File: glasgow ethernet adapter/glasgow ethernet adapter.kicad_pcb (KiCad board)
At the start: 4 copper layers, 61.7 x 49 mm, 60 parts, among them J1 Glasgow Port, J2 RJ45_Amphenol_RJMG201K21120FR, U1 MxL86110, Y1 25 MHz

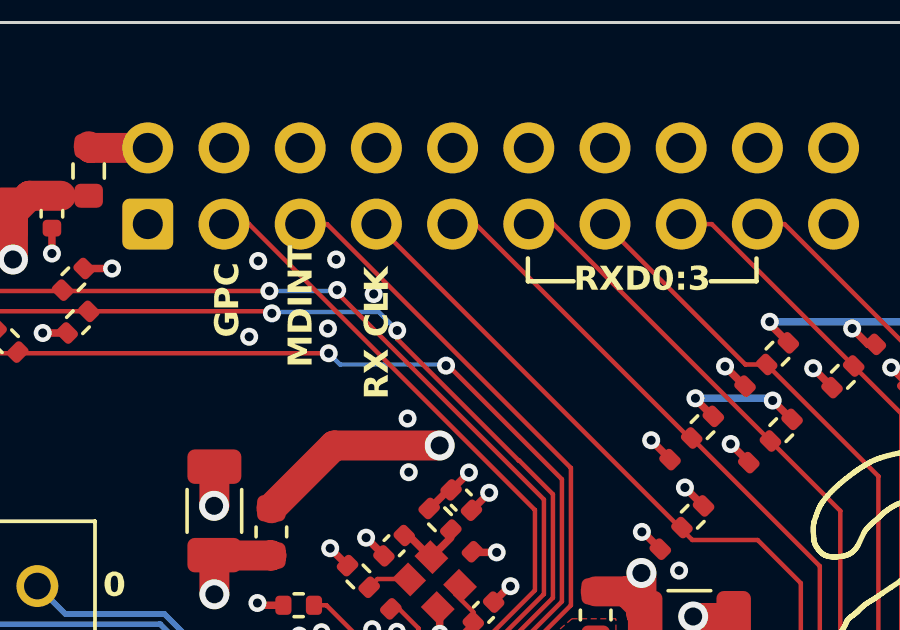
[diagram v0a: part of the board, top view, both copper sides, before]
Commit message: add RX_CTL silkscreen label
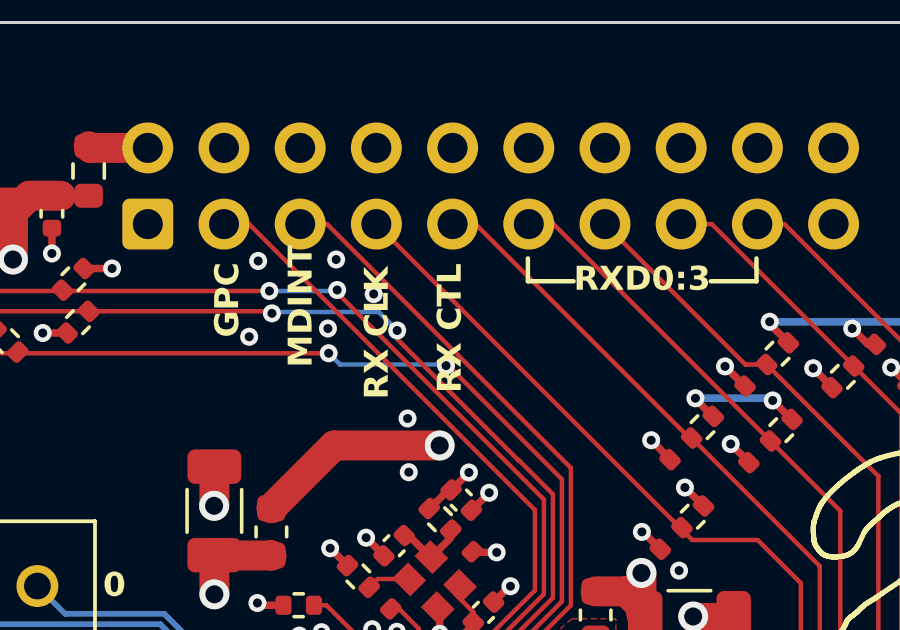
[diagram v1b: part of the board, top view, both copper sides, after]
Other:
- board text added: "RX CTL"
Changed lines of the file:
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@@
+		)
+	)
+	(gr_text "RX CTL\n"
+		(at 163.1 87.85 90)
+		(layer "F.SilkS")
+		(effects
+			(font
+				(size 0.8 0.8)
+				(thickness 0.15)
+				(bold yes)
+			)
+			(justify left bottom)
 		)
 	)

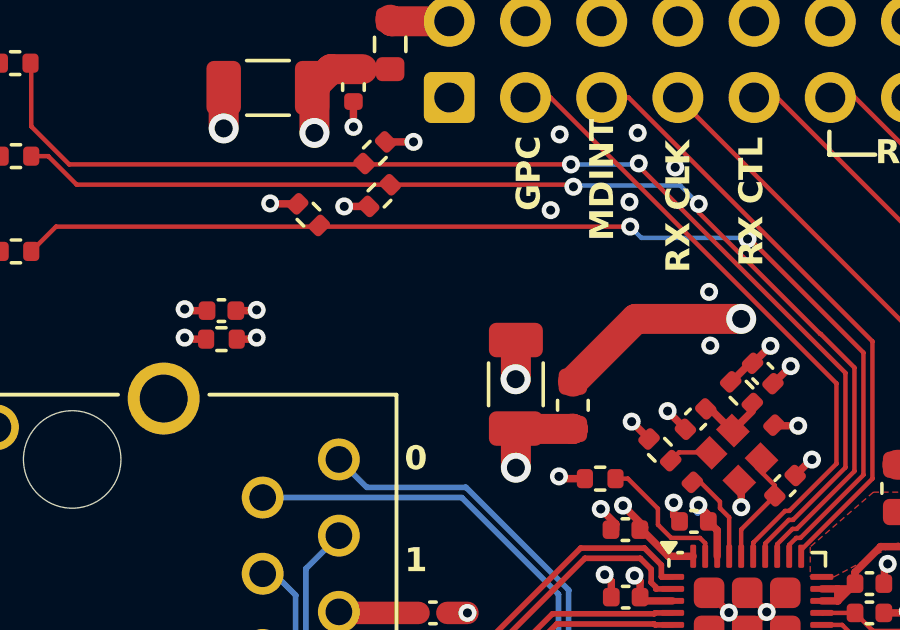
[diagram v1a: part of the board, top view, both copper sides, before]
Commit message: add 1v1 regulator
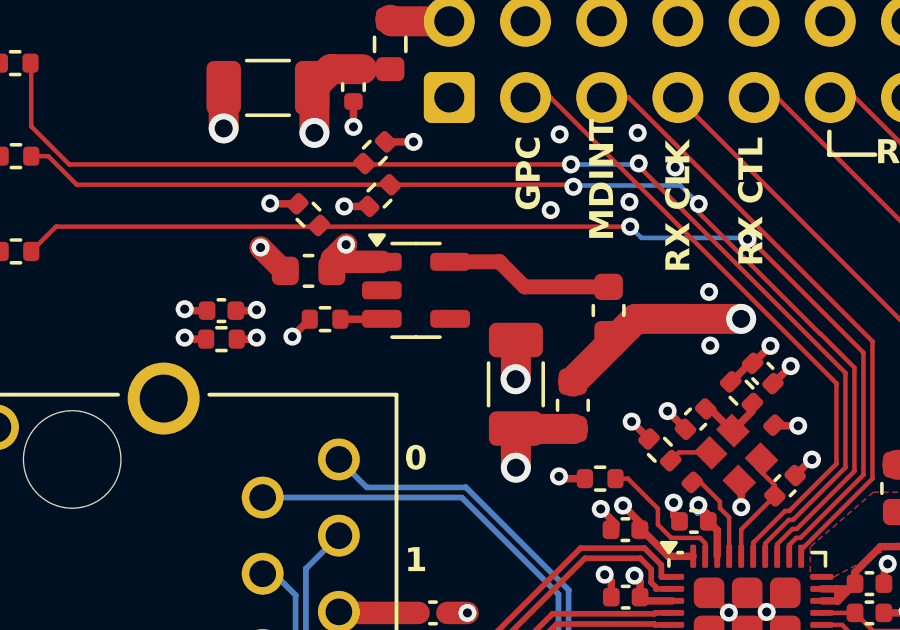
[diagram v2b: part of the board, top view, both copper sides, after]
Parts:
- added C16: 1u, Capacitor_SMD:C_0603_1608Metric, F.Cu at (147.9, 88.0)
- added L4: 2.2 uH, Inductor_SMD:L_0603_1608Metric, F.Cu at (157.9, 89.3)
- added R27: 4.7k, Resistor_SMD:R_0402_1005Metric, F.Cu at (148.4, 89.6)
- added U2: ~, Package_TO_SOT_SMD:SOT-23-5, F.Cu at (151.5, 88.6)
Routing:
- net Net-(U2-OUT): track 0.00 -> 5.64 mm
- net +3V3: track 36.0 -> 39.7 mm, vias 15 -> 17
- net Net-(U2-EN): track 0.00 -> 1.39 mm
- net GND: track 48.0 -> 49.2 mm, vias 50 -> 51

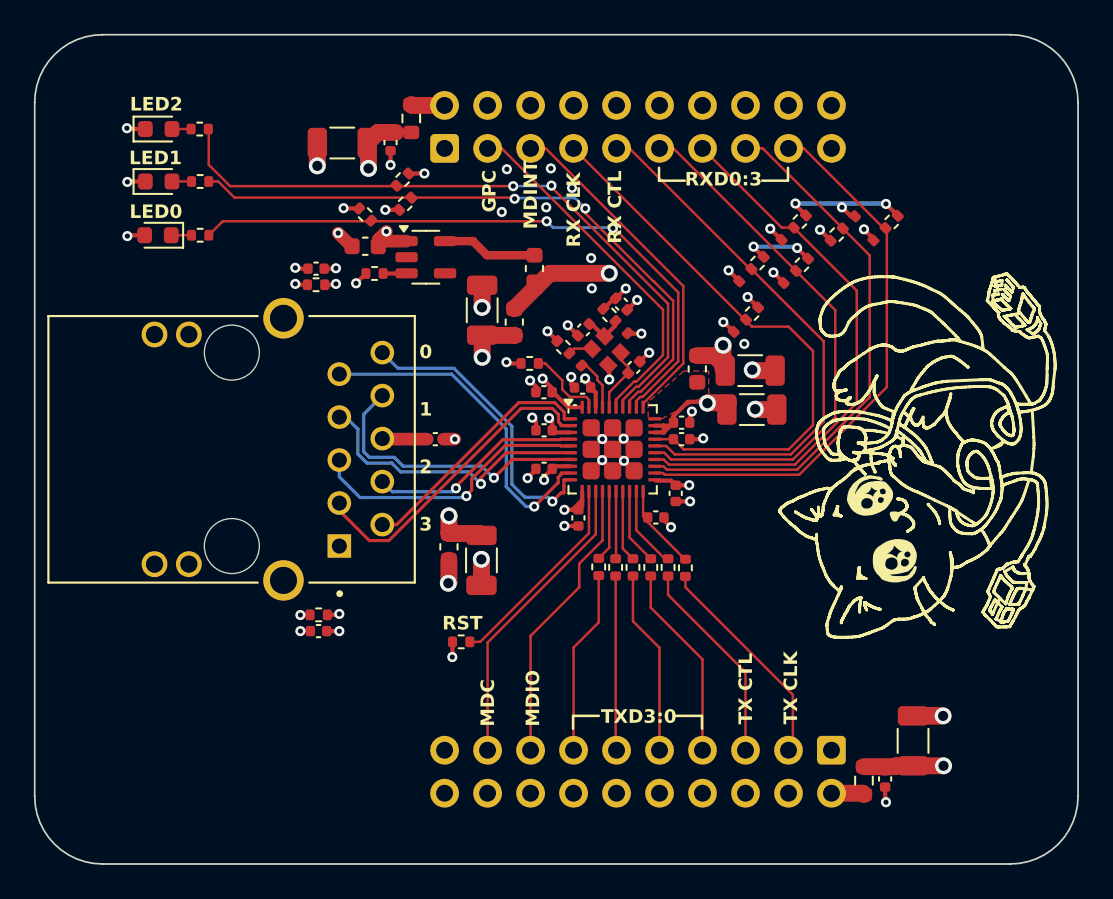
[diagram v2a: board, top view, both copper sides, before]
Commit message: swap MDC+MDIO with TXD0:3
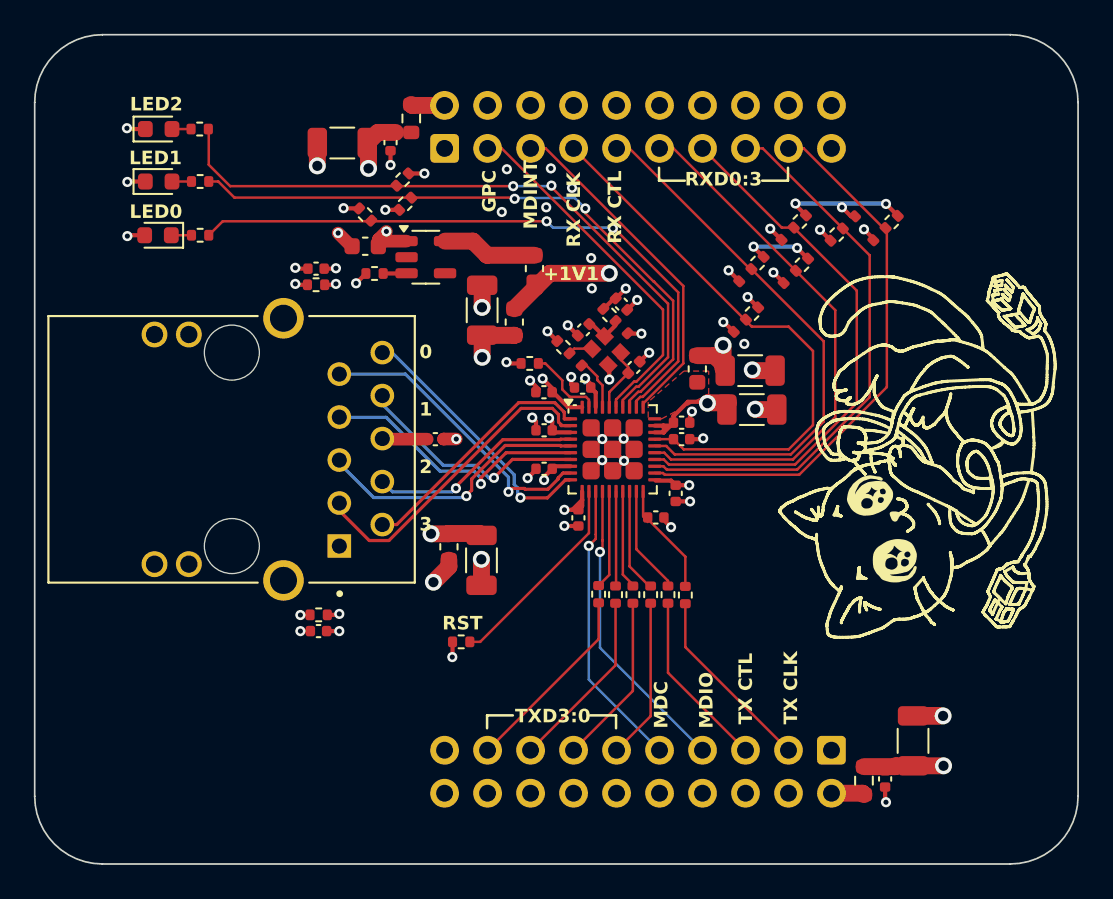
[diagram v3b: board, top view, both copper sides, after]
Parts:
- moved R15 1.61 mm to (161.7, 108.6)
- moved R16 1.61 mm to (162.7, 108.6)
- moved R23 1.61 mm to (166.8, 108.6)
- moved R20 1.61 mm to (163.7, 108.6)
- moved R21 1.61 mm to (164.7, 108.6)
- moved R22 1.61 mm to (165.8, 108.6)
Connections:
- J1 pad B2: /TXD0 -> /MDIO
- J1 pad B3: /TXD1 -> /MDC
- J1 pad B4: /TXD2 -> /TXD0
- J1 pad B5: /TXD3 -> /TXD1
- J1 pad B6: /MDIO -> /TXD2
- J1 pad B7: /MDC -> /TXD3
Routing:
- net /TRX3-: track 17.1 -> 13.9 mm
- net /TRX4+: track 20.4 -> 18.0 mm
- net /TRX4-: track 17.8 -> 15.7 mm
- net /TXD0: track 11.6 -> 9.60 mm
- net Net-(U1-TX_CLK): track 5.26 -> 7.15 mm
- net Net-(U1-TX_CTL): track 4.87 -> 6.55 mm
- net Net-(U1-TXD0): track 4.50 -> 6.16 mm
- net Net-(U1-TXD2): track 3.99 -> 5.60 mm
- net Net-(U1-TXD1): track 4.23 -> 5.83 mm
- net /TX_CTL: track 12.2 -> 10.6 mm
- net /TX_CLK: track 13.0 -> 11.6 mm
- net Net-(U1-TXD3): track 4.39 -> 5.82 mm
- net /MDIO: track 17.1 -> 17.9 mm, vias 0 -> 1
- net /TXD1: track 10.9 -> 10.1 mm
- net /MDC: track 17.9 -> 17.2 mm, vias 0 -> 1
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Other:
- board text added: "+1V1"

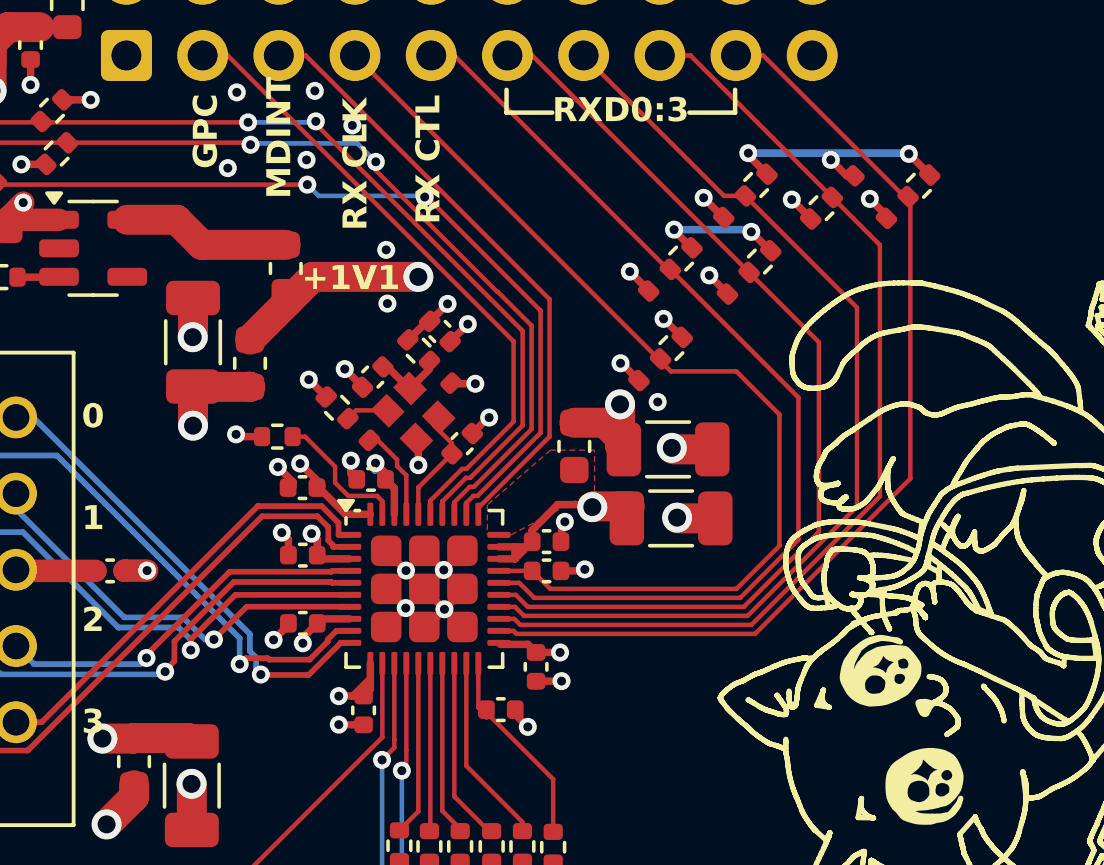
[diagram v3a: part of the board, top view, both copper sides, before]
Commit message: add Cout to +1v1, add to resistor silk
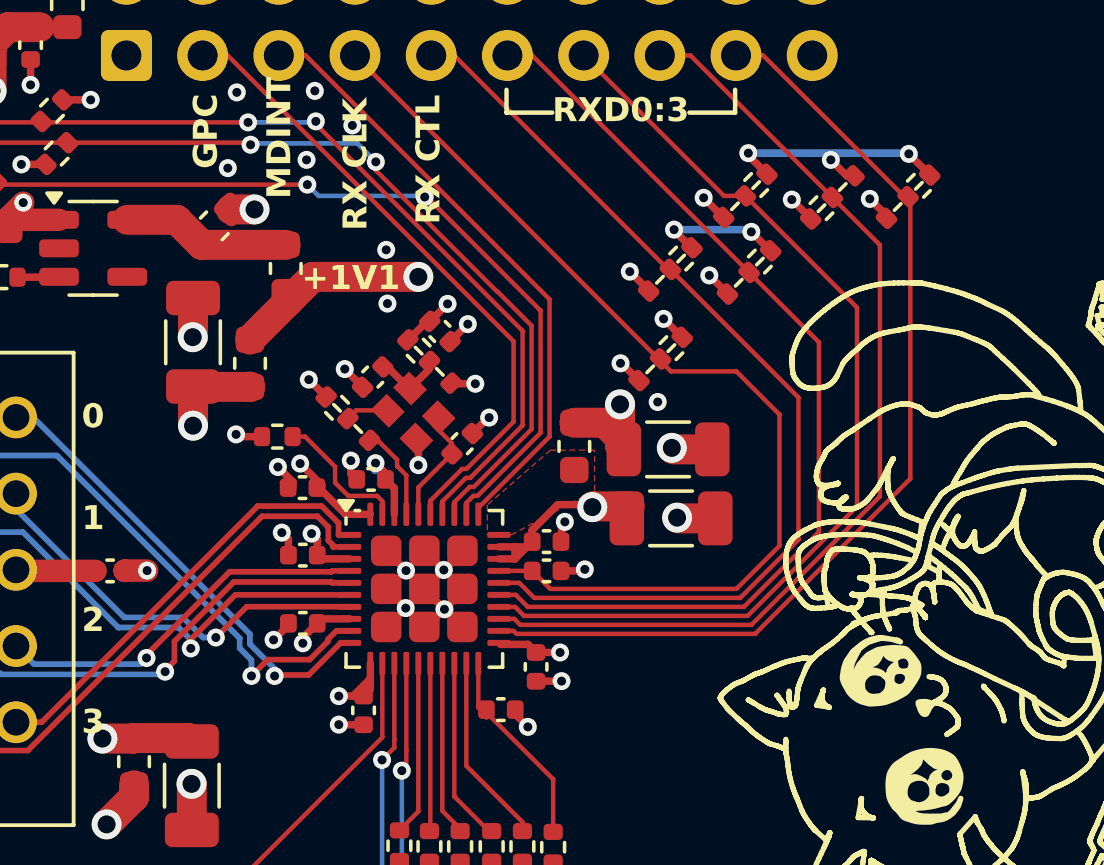
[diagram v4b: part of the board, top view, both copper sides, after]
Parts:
- added C18: 1u, Capacitor_SMD:C_0603_1608Metric, F.Cu at (155.5, 87.9)
- D1: value LED -> LED_0
- D2: value LED -> LED_1
- D3: value LED -> LED_3
- R17, R18, R19: value 150 -> 1k
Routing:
- net GND: track 49.2 -> 50.0 mm, vias 51 -> 52
